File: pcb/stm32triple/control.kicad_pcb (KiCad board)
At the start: 2 copper layers, 62 x 39.5 mm, 53 parts, among them J1 USB_C_Receptacle_USB2.0, J4 Term, J5 Term, J6 Term, P1 ST-Link, P2 ST-Link, P3 UG-2864ASWPG01, P4 har-flexicon 2,54 MSH-4, P5 har-flexicon 2,54 MSH-4, P6 har-flexicon 2,54 MSH-4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

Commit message: Control brightness and duraton with remote control
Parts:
- added C13: 100n, Capacitor_SMD:C_0603_1608Metric, F.Cu at (74.2, 127.0)
- added C14: 100n, Capacitor_SMD:C_0603_1608Metric, F.Cu at (75.4, 134.1)
- added D2: D_Photo, local:PhotoDiode, F.Cu at (78.0, 129.0)
- added U8: TSOP312xx, local:TSOP31238, F.Cu at (78.0, 131.2)
- P1: value ST-Link -> Conn_02x07_Odd_Even
- U4, U5, U6: footprint local:SP3485 -> local:SO-8
- moved C2 57.9 mm to (127.2, 113.5)
- moved R1 57.9 mm to (129.9, 112.9)
- moved R2 57.9 mm to (129.9, 110.4)
- moved U2 57.9 mm to (127.5, 110.8)
- moved C1 57.5 mm to (127.6, 108.0)
- moved JP1 16.4 mm to (86.4, 123.6)
- moved C4 6.96 mm to (82.0, 122.0)
- moved D1 4.00 mm to (78.0, 122.0)
- moved R5 2.44 mm to (85.8, 116.7)
- moved U7 2.20 mm to (78.0, 124.2)
- moved REF** 1.00 mm to (70.0, 122.0)
- renumbered C13 to C15, C14 to C16, C15 to C17
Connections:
- P1 pad 6: SWCLK -> SDCLK
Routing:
- net GND: track 324.8 -> 364.6 mm, vias 22 -> 24
- net VBUS: track 33.9 -> 21.3 mm
- net IR: track 21.3 -> 26.2 mm
- net +3V3: track 248.3 -> 246.2 mm
- net RS485_TX: track 25.6 -> 27.0 mm
- net RS485_RX: track 44.2 -> 45.3 mm
- net RS485_DE: track 27.0 -> 27.9 mm
- net +15V: track 94.2 -> 93.4 mm
- net BS: track 30.0 -> 30.4 mm, vias 2 -> 1
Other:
- board size 62 x 39.5 mm -> 64 x 39.5 mm

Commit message: Add SnowSparkle, new footprints
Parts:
- removed J4, J5, J6: Term, local:Termination
- added R11: 120R, local:1206-term, F.Cu at (79.4, 108.7)
- added R12: 120R, local:1206-term, F.Cu at (81.4, 108.7)
- added R13: 120R, local:1206-term, F.Cu at (87.7, 104.8)
- added R14: 120R, local:1206-term, F.Cu at (89.7, 104.8)
- added R15: 120R, local:1206-term, F.Cu at (121.5, 108.4)
- added R16: 120R, local:1206-term, F.Cu at (123.5, 108.4)
- C1, C3: footprint Capacitor_SMD:C_1206_3216Metric -> local:1206
- C10, C11, C12, C13, C14, C15, C16, C17, C4, C5, C6: footprint Capacitor_SMD:C_0603_1608Metric -> local:0603
- C2: footprint Capacitor_SMD:C_0805_2012Metric -> local:0805
- P1: value Conn_02x07_Odd_Even -> FTSH-107-01-L-DV-K; footprint local:FTSH-107-01-L-DV-K -> local:PinHeader-2x7-1.27mm-smd
- P3: value UG-2864ASWPG01 -> AFC07-S24FCC-00; footprint local:Connector-Flat-24_P0.5mm -> local:Connector-Flat-24-0.5mm
- R1, R10, R2, R3, R4, R5, R6, R7, R8, R9: footprint Resistor_SMD:R_0603_1608Metric -> local:0603
- moved C3 1.03 mm to (110.6, 115.2)
- moved P3 0.35 mm to (100.0, 111.2)
- moved R3 0.16 mm to (113.9, 118.7)
- turned U2 to 0 degrees
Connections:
- P1 pad 6: SDCLK -> SWCLK
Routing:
- net GND: track 364.6 -> 365.9 mm

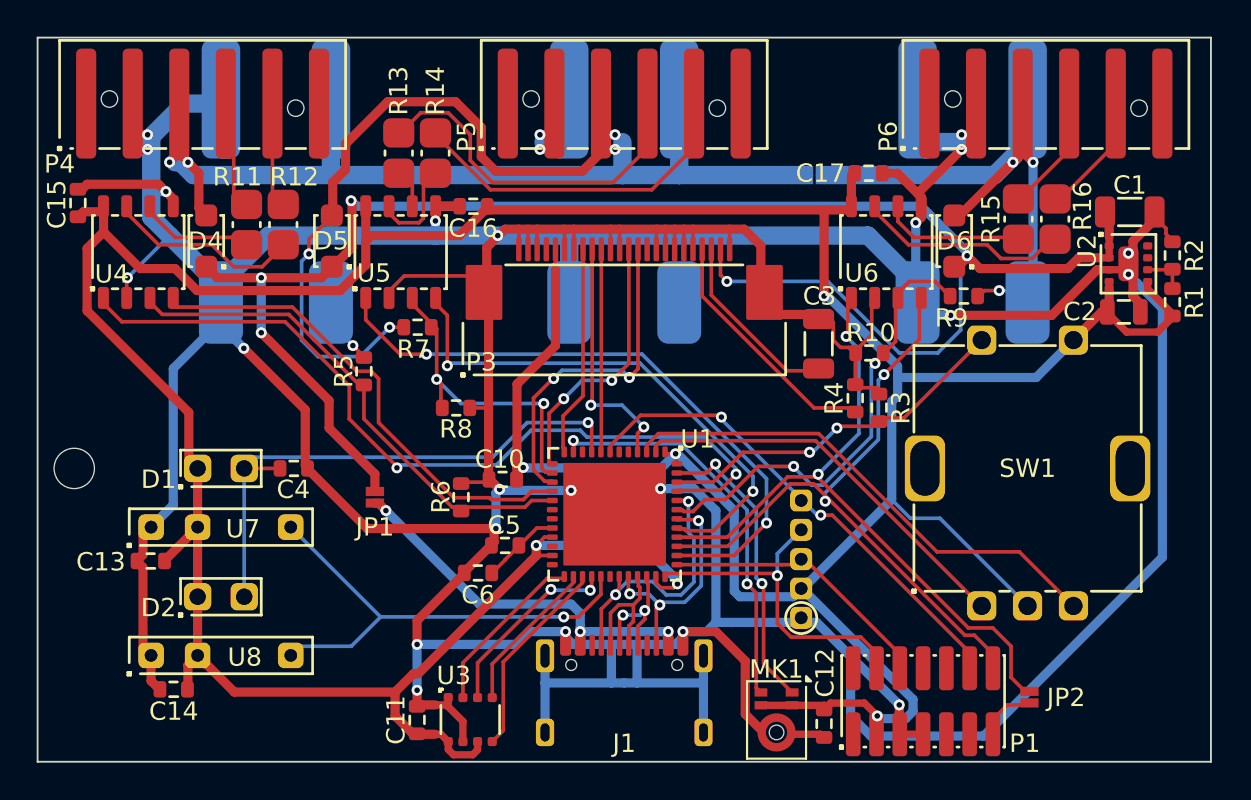
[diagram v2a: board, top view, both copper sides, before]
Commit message: Use TSOP38338
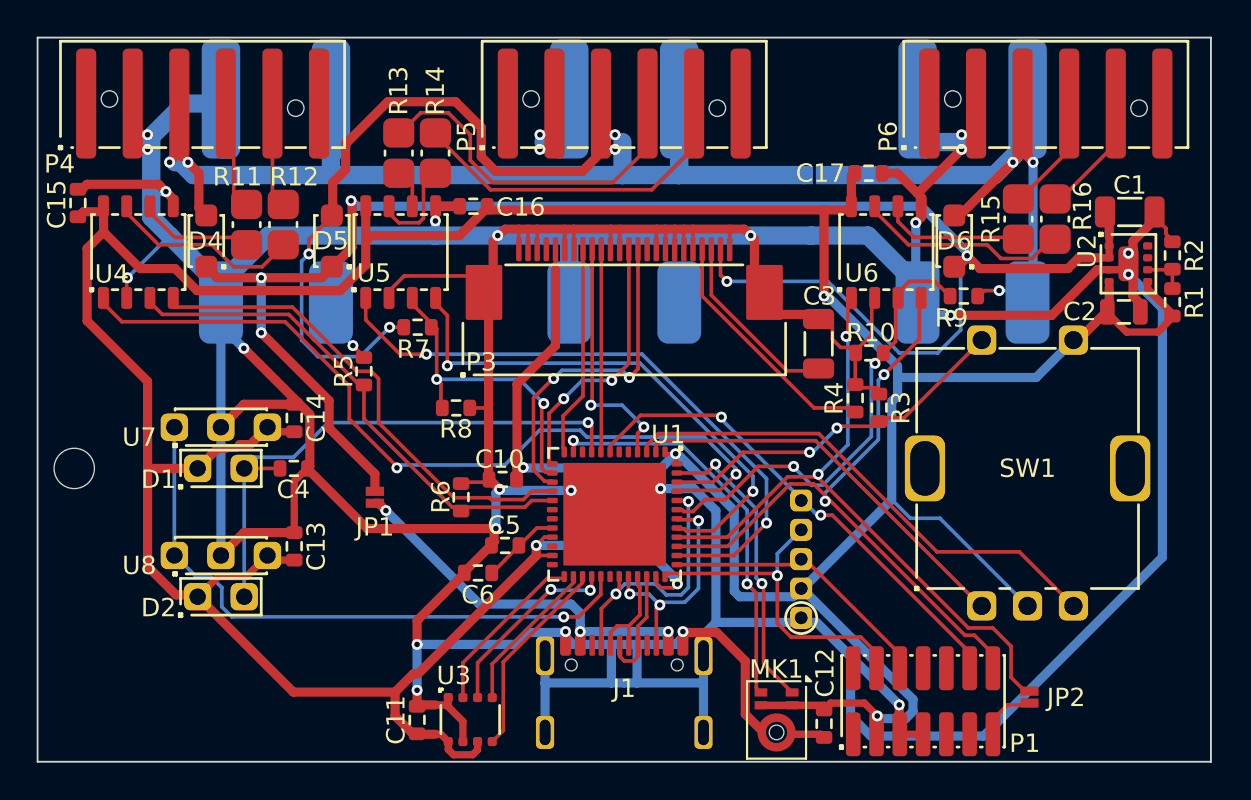
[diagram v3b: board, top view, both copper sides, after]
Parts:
- J1: footprint local:USB4105-GF-A-120 -> local:TYPE-C-16PIN-2MD-073
- U1: footprint local:STM32G431CBU -> local:STM32-UFQFPN48
- U7, U8: value TSOP312xx -> TSOP38338; footprint local:TSOP31238 -> local:TSOP38338
- moved C14 16.2 mm to (82.0, 119.2), turned to 90 degrees
- moved C13 7.87 mm to (82.0, 126.2), turned to 90 degrees
- moved J1 5.00 mm to (100.0, 134.0)
- moved U7 4.95 mm to (78.0, 119.2)
- moved U8 4.95 mm to (78.0, 126.2)
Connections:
- U7 pad 1: GND -> IR
- U7 pad 2: +3V3 -> GND
- U7 pad 3: IR -> +3V3
- U8 pad 1: GND -> IR
- U8 pad 2: +3V3 -> GND
- U8 pad 3: IR -> +3V3
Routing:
- net +3V3: track 246.2 -> 255.7 mm
- net IR: track 26.2 -> 33.8 mm
- net GND: track 365.9 -> 372.8 mm, vias 24 -> 25
- net USB_DM: track 7.38 -> 5.98 mm
- net USB_DP: track 7.15 -> 6.44 mm, vias 2 -> 0
